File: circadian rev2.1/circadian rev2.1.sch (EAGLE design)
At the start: 246 parts, among them IC1 4017D, IC10 LM4040B05, IC2 4051D, IC3 4051D, IC4 74HC595D, IC5 4053D, IC6 74HC595D, IC7 4051D, IC8 FT232RL, IC9 LM4040B10

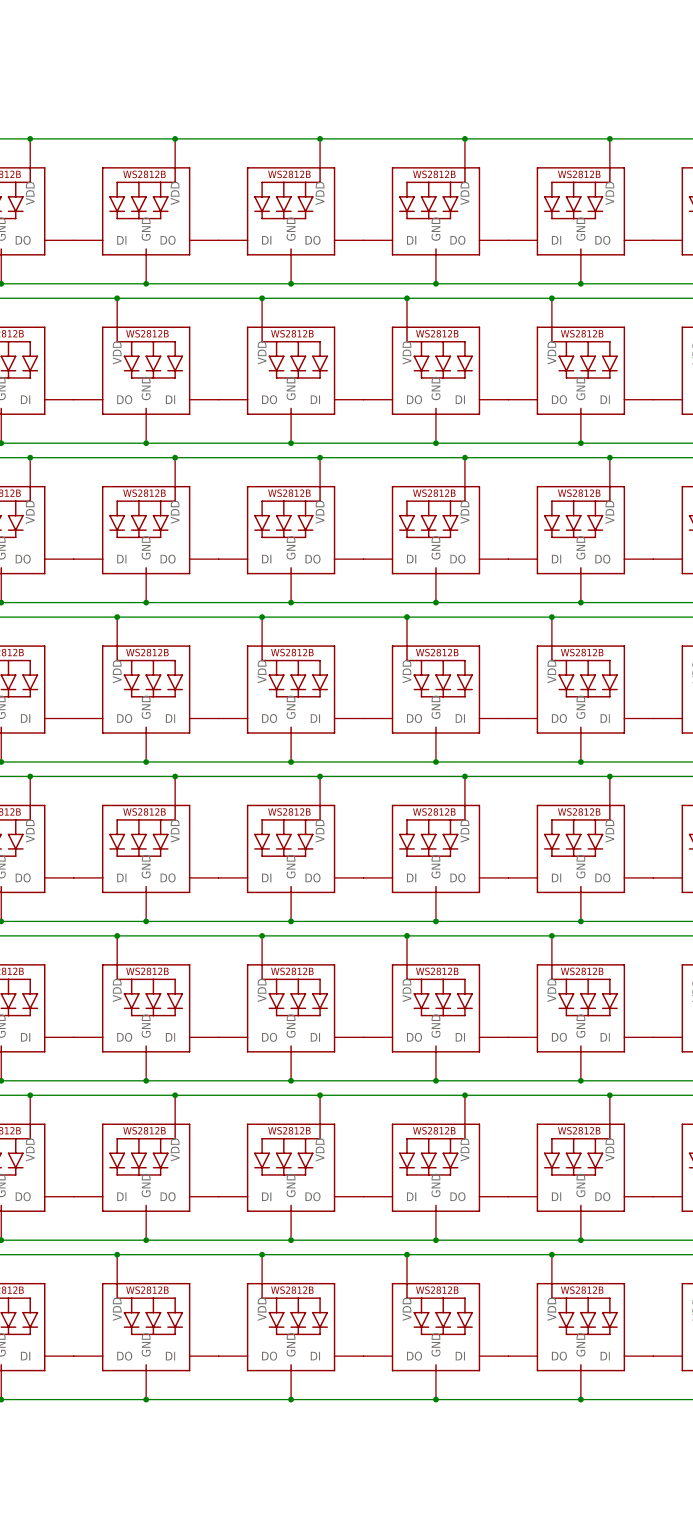
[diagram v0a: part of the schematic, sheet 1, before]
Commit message: Fixed wrong LED type causing confusion
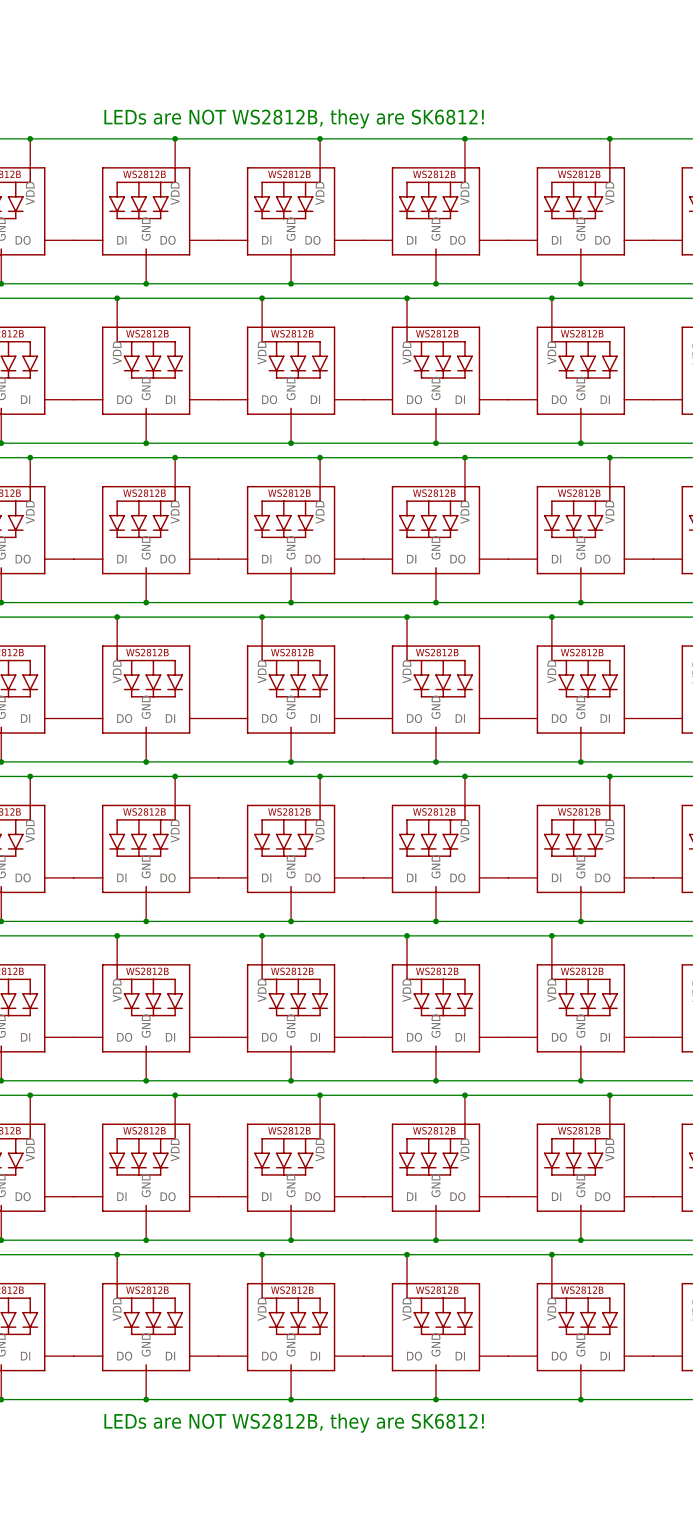
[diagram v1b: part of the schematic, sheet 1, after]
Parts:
- LED1, LED10, LED11, LED12, LED13, LED14, LED15, LED16, LED17, LED18, LED19, LED2, LED20, LED21, LED22, LED23, LED24, LED25, LED26, LED27, LED28, LED29, LED3, LED30, LED31, LED32, LED33, LED34, LED35, LED36, LED37, LED38, LED39, LED4, LED40, LED41, LED42, LED43, LED44, LED45, LED46, LED47, LED48, LED49, LED5, LED50, LED51, LED52, LED53, LED54, LED55, LED56, LED57, LED58, LED59, LED6, LED60, LED61, LED62, LED63, LED64, LED65, LED66, LED67, LED68, LED69, LED7, LED70, LED71, LED72, LED8, LED9: value WS2812B3535 -> SK68123535
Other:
- note added: "LEDs are NOT WS2812B, they are SK6812!"
